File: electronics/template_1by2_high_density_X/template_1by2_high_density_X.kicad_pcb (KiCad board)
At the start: 2 copper layers, 19 x 19 mm, 8 parts, among them J1 1, J2 2, J3 3, J4 4, J5 5, J6 6

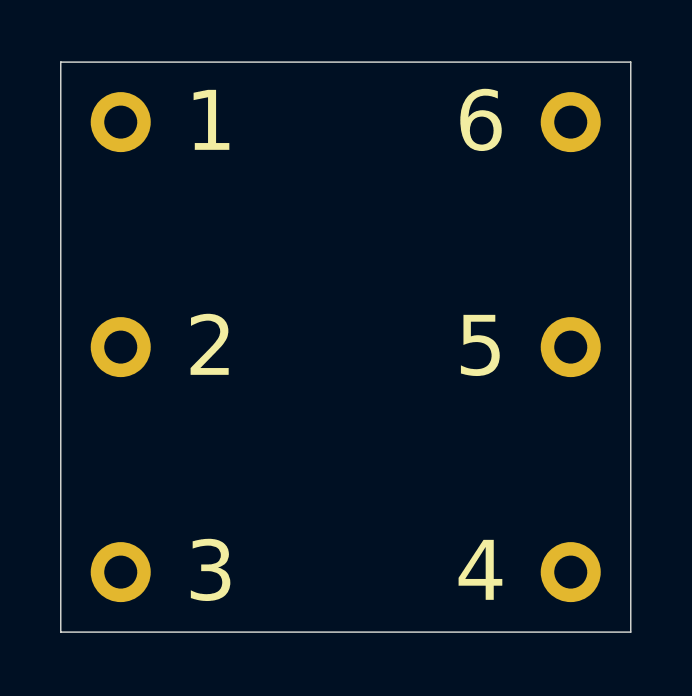
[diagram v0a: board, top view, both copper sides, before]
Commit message: completed high density X templates, updated versionnumbers of high density XN templates
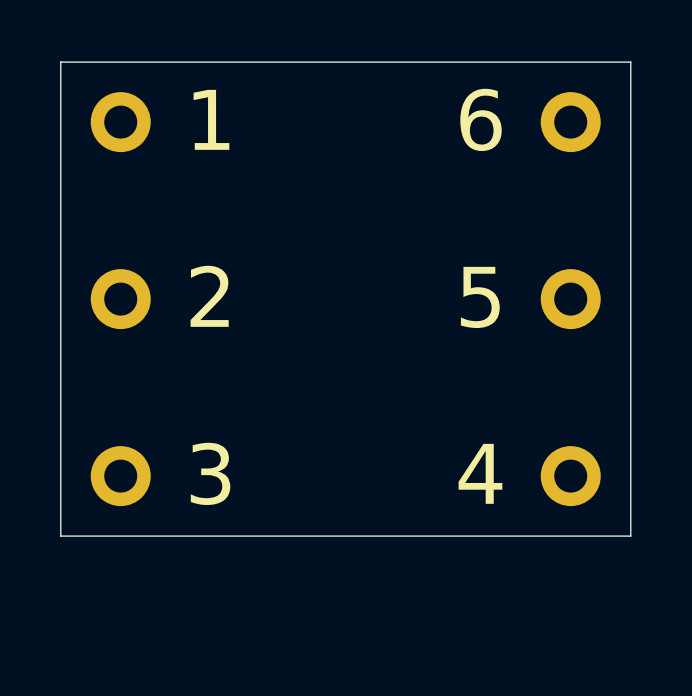
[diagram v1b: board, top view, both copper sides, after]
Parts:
- N1: value V20220113 -> V20240506
- moved J3 3.20 mm to (142.5, 74.3)
- moved J4 3.20 mm to (157.5, 74.3)
- moved J2 1.60 mm to (142.5, 68.4)
- moved J5 1.60 mm to (157.5, 68.4)
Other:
- board size 19 x 19 mm -> 19 x 15.8 mm
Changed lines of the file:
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@@
   )
   (net 0 "")
-  (net 1 "Net-(J1-Pad1)")
+  (net 1 "Net-(J1-Pin_1)")
   (footprint "mill-max:PC_pin_nail_head_6092" locked (layer "F.Cu")
     (at 142.5 62.5)
+    (property "Sheetfile" "template_1by2_high_density_X.kicad_sch")
+    (property "Sheetname" "")
+    (property "ki_description" "Generic connector, single row, 01x01, script generated (kicad-library-utils/schlib/autogen/connector/)")
+    (property "ki_keywords" "connector")
     (attr through_hole)
     (fp_text reference "J1" (at 3 0) (layer "F.Fab")
@@
       (stroke (width 0.025) (type solid)) (fill none) (layer "F.CrtYd"))
     (pad "1" thru_hole circle locked (at 0 0) (size 2 2) (drill 1.1) (layers "*.Cu" "*.Mask")
-      (net 1 "Net-(J1-Pad1)"))
+      (net 1 "Net-(J1-Pin_1)") (pinfunction "Pin_1") (pintype "passive"))
   )
   (footprint "mill-max:PC_pin_nail_head_6092" locked (layer "F.Cu")
-    (at 142.5 70)
+    (at 142.5 68.4)
+    (property "Sheetfile" "template_1by2_high_density_X.kicad_sch")
+    (property "Sheetname" "")
+    (property "ki_description" "Generic connector, single row, 01x01, script generated (kicad-library-utils/schlib/autogen/connector/)")
+    (property "ki_keywords" "connector")
     (attr through_hole)
     (fp_text reference "J2" (at 3 0) (layer "F.Fab")
@@
       (stroke (width 0.025) (type solid)) (fill none) (layer "F.CrtYd"))
     (pad "1" thru_hole circle locked (at 0 0) (size 2 2) (drill 1.1) (layers "*.Cu" "*.Mask")
-      (net 1 "Net-(J1-Pad1)"))
+      (net 1 "Net-(J1-Pin_1)") (pinfunction "Pin_1") (pintype "passive"))
   )
   (footprint "mill-max:PC_pin_nail_head_6092" locked (layer "F.Cu")
-    (at 142.5 77.5)
+    (at 142.5 74.3)
+    (property "Sheetfile" "template_1by2_high_density_X.kicad_sch")
+    (property "Sheetname" "")
+    (property "ki_description" "Generic connector, single row, 01x01, script generated (kicad-library-utils/schlib/autogen/connector/)")
+    (property "ki_keywords" "connector")
     (attr through_hole)
     (fp_text reference "J3" (at 3 0) (layer "F.Fab")
@@
       (stroke (width 0.025) (type solid)) (fill none) (layer "F.CrtYd"))
     (pad "1" thru_hole circle locked (at 0 0) (size 2 2) (drill 1.1) (layers "*.Cu" "*.Mask")
-      (net 1 "Net-(J1-Pad1)"))
+      (net 1 "Net-(J1-Pin_1)") (pinfunction "Pin_1") (pintype "passive"))
   )
   (footprint "mill-max:PC_pin_nail_head_6092" locked (layer "F.Cu")
-    (at 157.5 70)
+    (at 157.5 68.4)
+    (property "Sheetfile" "template_1by2_high_density_X.kicad_sch")
+    (property "Sheetname" "")
+    (property "ki_description" "Generic connector, single row, 01x01, script generated (kicad-library-utils/schlib/autogen/connector/)")
+    (property "ki_keywords" "connector")
     (attr through_hole)
     (fp_text reference "J5" (at -3 0) (layer "F.Fab")
@@
       (stroke (width 0.025) (type solid)) (fill none) (layer "F.CrtYd"))
     (pad "1" thru_hole circle locked (at 0 0) (size 2 2) (drill 1.1) (layers "*.Cu" "*.Mask")
-      (net 1 "Net-(J1-Pad1)"))
+      (net 1 "Net-(J1-Pin_1)") (pinfunction "Pin_1") (pintype "passive"))
   )
   (footprint "mill-max:PC_pin_nail_head_6092" locked (layer "F.Cu")
     (at 157.5 62.5)
+    (property "Sheetfile" "template_1by2_high_density_X.kicad_sch")
+    (property "Sheetname" "")
+    (property "ki_description" "Generic connector, single row, 01x01, script generated (kicad-library-utils/schlib/autogen/connector/)")
+    (property "ki_keywords" "connector")
     (attr through_hole)
     (fp_text reference "J6" (at -3 0) (layer "F.Fab")
@@
       (stroke (width 0.025) (type solid)) (fill none) (layer "F.CrtYd"))
     (pad "1" thru_hole circle locked (at 0 0) (size 2 2) (drill 1.1) (layers "*.Cu" "*.Mask")
-      (net 1 "Net-(J1-Pad1)"))
+      (net 1 "Net-(J1-Pin_1)") (pinfunction "Pin_1") (pintype "passive"))
   )
   (footprint "mill-max:PC_pin_nail_head_6092" locked (layer "F.Cu")
-    (at 157.5 77.5)
+    (at 157.5 74.3)
+    (property "Sheetfile" "template_1by2_high_density_X.kicad_sch")
+    (property "Sheetname" "")
+    (property "ki_description" "Generic connector, single row, 01x01, script generated (kicad-library-utils/schlib/autogen/connector/)")
+    (property "ki_keywords" "connector")
     (attr through_hole)
     (fp_text reference "J4" (at -3 0) (layer "F.Fab")
@@
       (stroke (width 0.025) (type solid)) (fill none) (layer "F.CrtYd"))
     (pad "1" thru_hole circle locked (at 0 0) (size 2 2) (drill 1.1) (layers "*.Cu" "*.Mask")
-      (net 1 "Net-(J1-Pad1)"))
+      (net 1 "Net-(J1-Pin_1)") (pinfunction "Pin_1") (pintype "passive"))
   )
   (footprint "Symbol:OSHW-Symbol_6.7x6mm_SilkScreen" (layer "B.Cu")
@@
     (descr "Open Source Hardware Symbol")
     (tags "Logo Symbol OSHW")
-    (attr exclude_from_pos_files exclude_from_bom)
+    (property "Sheetfile" "template_1by2_high_density_X.kicad_sch")
+    (property "Sheetname" "")
+    (attr exclude_from_pos_files)
     (fp_text reference "N2" (at 0 0) (layer "B.SilkS") hide
         (effects (font (size 1 1) (thickness 0.15)) (justify mirror))
@@
     (descr "Label for general purpose use")
     (tags "Label")
+    (property "Sheetfile" "template_1by2_high_density_X.kicad_sch")
+    (property "Sheetname" "")
     (attr smd)
     (fp_text reference "N1" (at 0 -1.85) (layer "B.Fab") hide
         (effects (font (size 1 1) (thickness 0.15)) (justify mirror))
     )
-    (fp_text value "V20220113" (at 0.8 0.1) (layer "B.SilkS")
+    (fp_text value "V20240506" (at 0.8 0.1) (layer "B.SilkS")
         (effects (font (size 0.8 0.8) (thickness 0.15)) (justify mirror))
     )
@@
       (stroke (width 0.15) (type solid)) (layer "B.SilkS"))
   )
-  (gr_line (start 140.5 79.5) (end 159.5 79.5)
+  (gr_line (start 140.5 76.3) (end 159.5 76.3)
     (stroke (width 0.05) (type solid)) (layer "Edge.Cuts"))
-  (gr_line (start 159.5 60.5) (end 159.5 79.5)
+  (gr_line (start 159.5 60.5) (end 159.5 76.3)
     (stroke (width 0.05) (type solid)) (layer "Edge.Cuts"))
   (gr_line (start 159.5 60.5) (end 140.5 60.5)
     (stroke (width 0.05) (type solid)) (layer "Edge.Cuts"))
-  (gr_line (start 140.5 79.5) (end 140.5 60.5)
+  (gr_line (start 140.5 76.3) (end 140.5 60.5)
     (stroke (width 0.05) (type solid)) (layer "Edge.Cuts"))
 )
